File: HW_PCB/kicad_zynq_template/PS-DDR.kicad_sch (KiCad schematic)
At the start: 1 part, among them U2 XA7Z020-1CLG400I

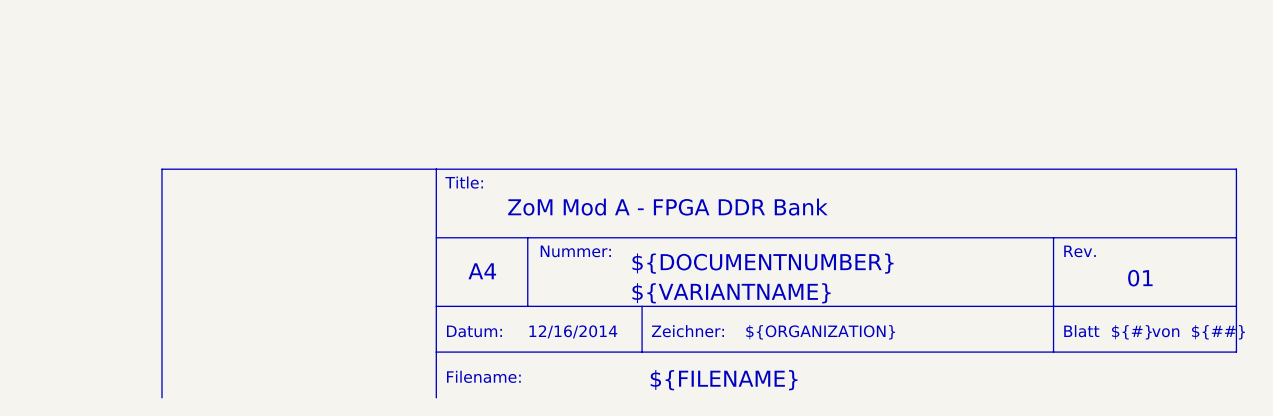
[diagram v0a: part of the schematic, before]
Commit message: pcbs tidied up
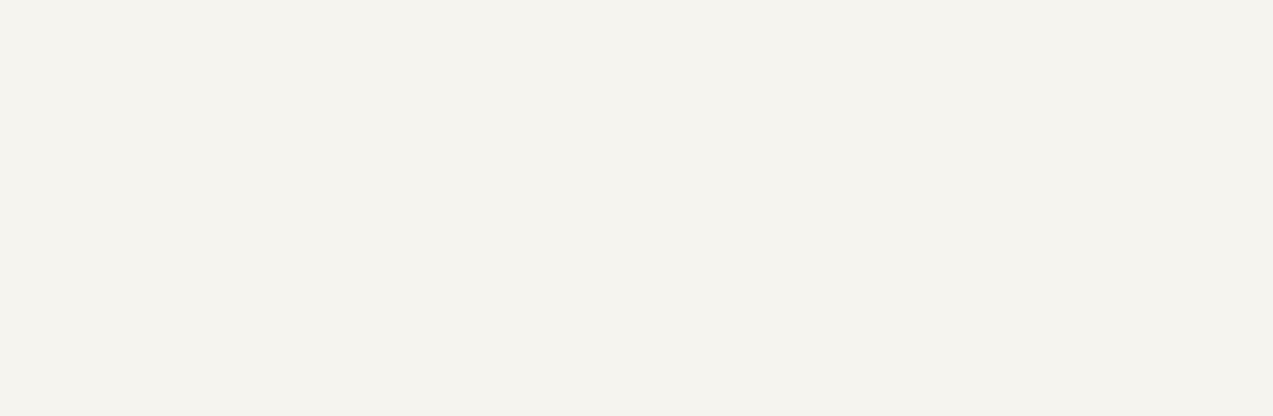
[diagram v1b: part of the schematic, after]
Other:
- note removed: "${##}"
- note removed: "${#}"
- note removed: "${DOCUMENTNUMBER}"
- note removed: "${FILENAME}"
- note removed: "${ISSUE_DATE}"
- note removed: "${ORGANIZATION}"
- note removed: "${REVISION}"
- note removed: "${TITLE}"
- note removed: "${VARIANTNAME}"
- note removed: "A4"
- note removed: "Blatt"
- note removed: "Datum:"
- note removed: "Filename:"
- note removed: "Nummer:"
- note removed: "Rev."
- note removed: "Title:"
- note removed: "Zeichner:"
- note removed: "von"
